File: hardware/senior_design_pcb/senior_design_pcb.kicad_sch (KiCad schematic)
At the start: 103 parts, among them J1 SBH11-PBPC-D05-ST-BK, J10 Conn_01x04_Socket, J11 2x08Rectangle-LED Matrix Conn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, J12 1x05JST - Joystick2 connector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, J13 UJ20-C-H-C-4-SMT-TR, J2 Conn_01x08_Pin, J3 Conn_01x02_Socket, J4 Conn_01x02_Socket, J5 1x05JST-Admin LCD Console Con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, J6 1x05JST - Joystick1 connector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, J9 Conn_01x04_Socket, SW3 1x02JST-Admin Console button 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, U1 KMR241GLFS, U10 KMR241GLFS, U2 STM32F091RCTx, U3 LD1117S33TR_SOT223, U4 KMR241GLFS, U5 USBLC6-2SC6Y, U6 2SA1873-GRTE85L_F, U7 2SA1873-GRTE85L_F, U8 2SA1873-GRTE85L_F, U9 KMR241GLFS

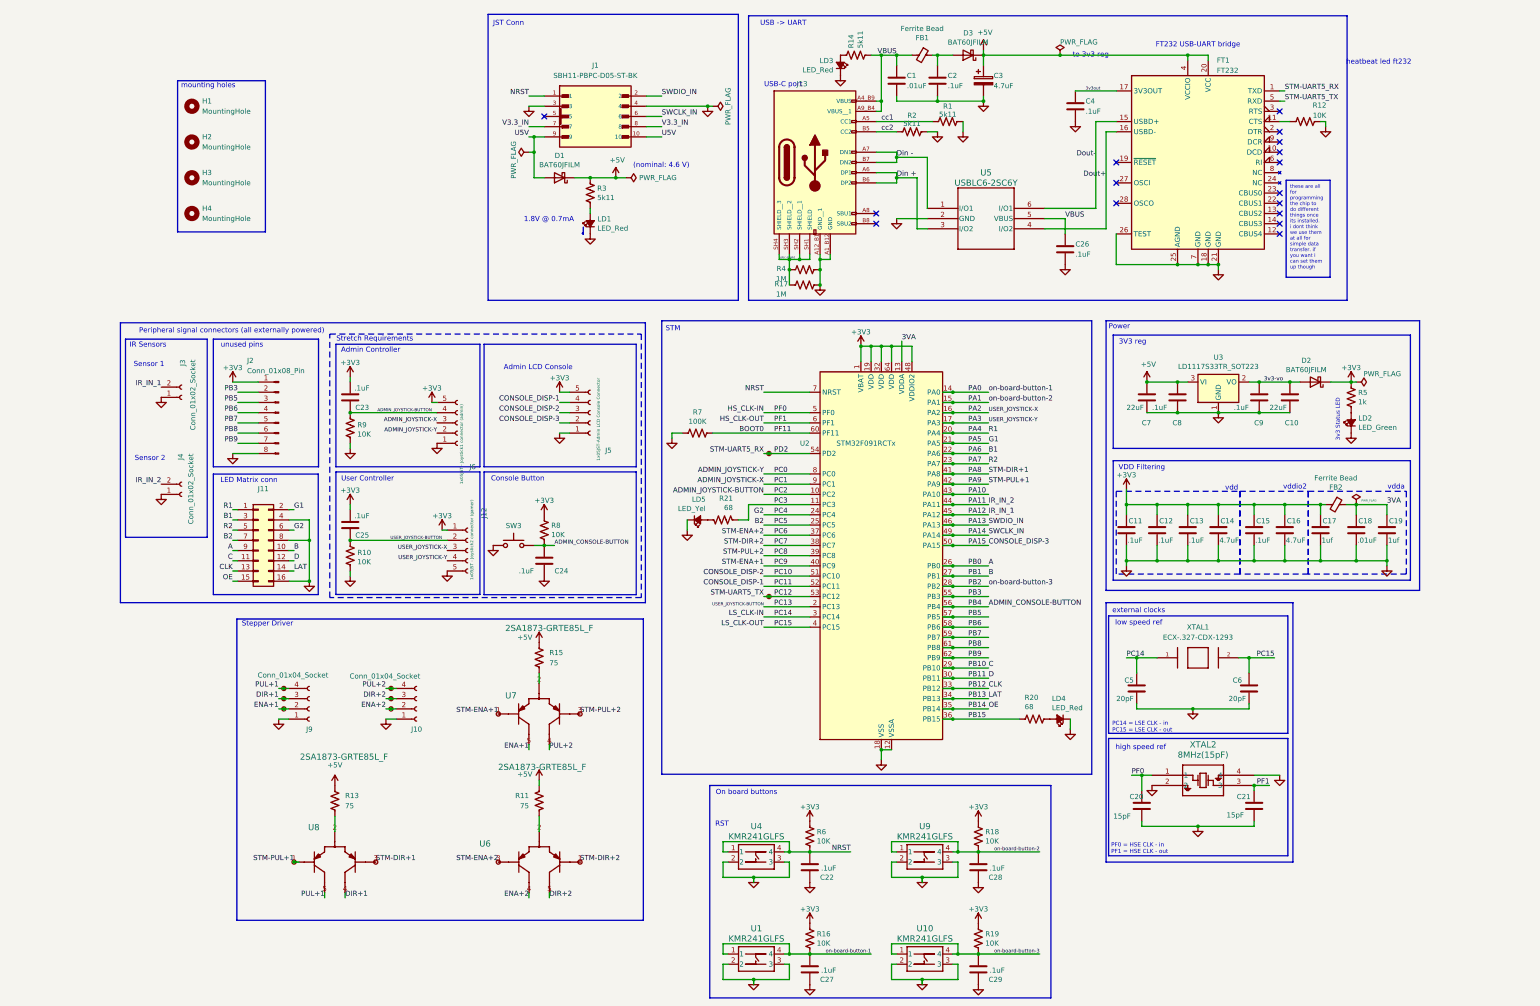
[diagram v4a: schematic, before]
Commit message: updated pcb
changes:
-all suggested from Setsuna & Shivam & presentation feedback
	-removed r4 and r17
	-kept multiple net names (following PCB Design Techniques - Spring 2025 from brightspace)
	-fixed XTAL1 missing connection
	-removed PWR_FLAG on GND
	-removed D2 - no need
	-increased via hole size (15 mil drill + 28 mil diameter)
	-kept chamfer (compared prices on jlc and pcbway and same price)
	-removed via on SW3
	-did not change traces beneath oscillators, everythings already routed but will keep in mind for the future
	-moved silkscreen names from off the board to on the board (we are still discussing decorative designs - if we include any)
	-kept FB since FB should be near source of noise and source of noise we are trying to prevent is from the USB-C. if we are misunderstanding this please let us know.
	-trace clearances updated, needed more with via size increase
	-moved silkscren + labeled pins
	-removed 3v connection from stlink. keeping only 5v

	-also, the led matrix connector somehow relapsed and changed to the 2x08 default header instead of a jtag type rectangular connector. updated and fixed :)

From prof. walters feedback:
-added back shield resistor
-added tvs diodes for joystick + buttons
-changed decoupling cap value
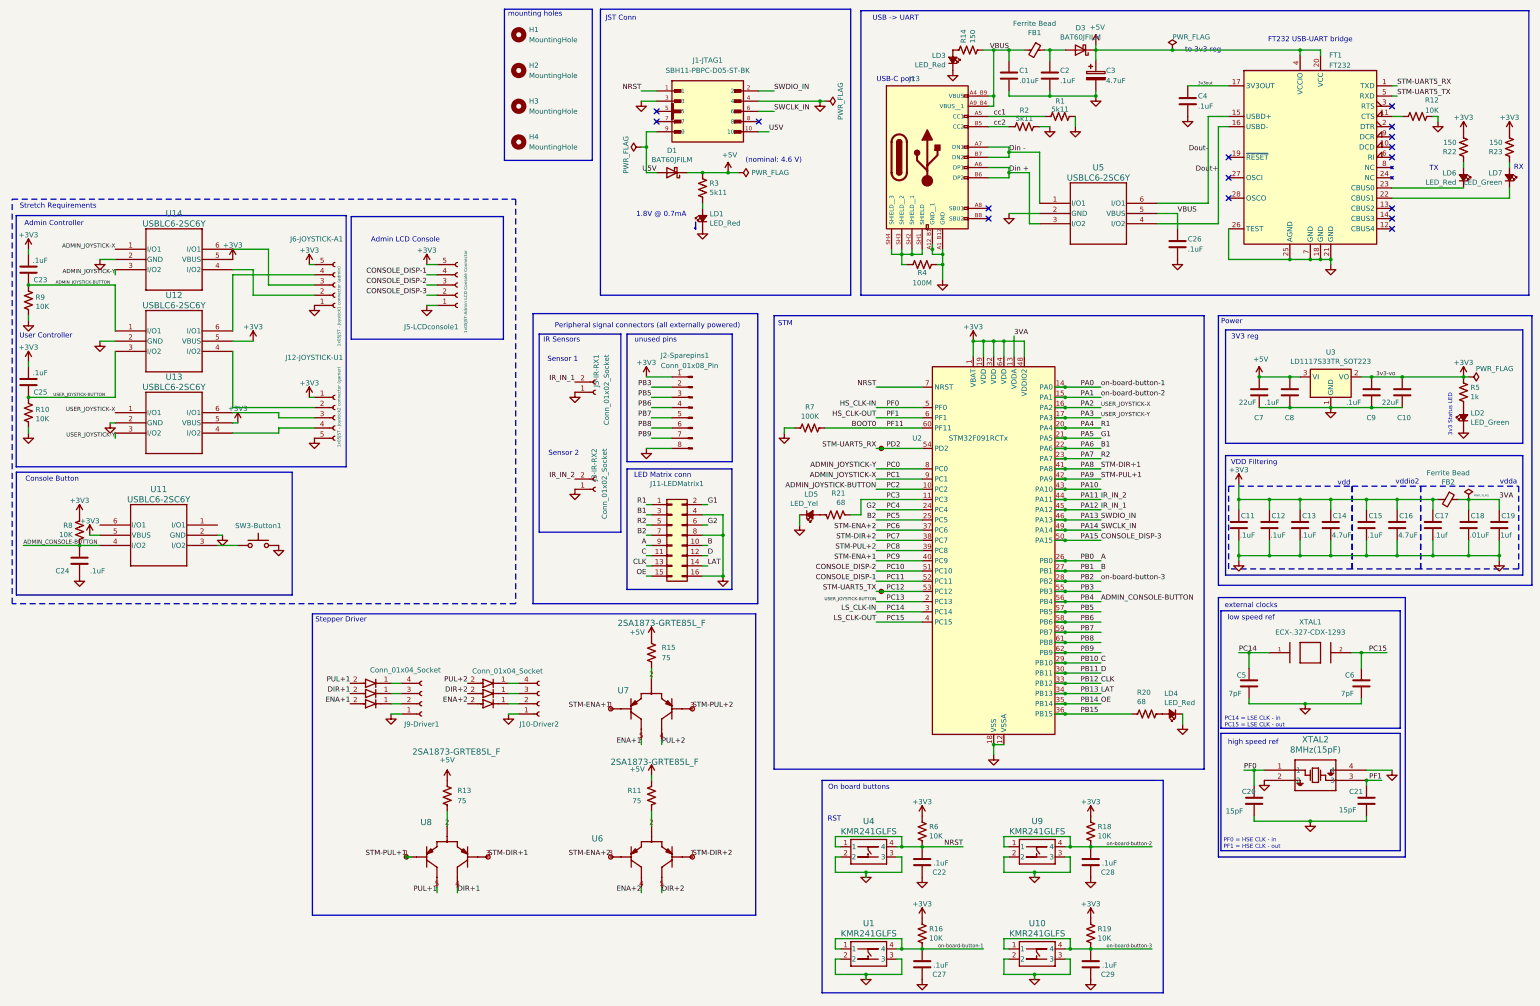
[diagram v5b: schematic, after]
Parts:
- removed D2: BAT60JFILM, Diode_SMD:D_SOD-323_HandSoldering, symbol Diode:BAT60A
- removed R17: 1M, Resistor_SMD:R_0805_2012Metric_Pad1.20x1.40mm_HandSolder, symbol Device:R_US
- removed TP1, TP2, TP3, TP4, TP5, TP6: TestPoint_Small, TestPoint:TestPoint_THTPad_D1.0mm_Drill0.5mm, symbol testpoint:TestPoint_Small
- added CR1, CR2, CR3, CR4, CR5, CR6: JAN1N4148UR-1, kicad_library:jan1n4148 smd diode-M, symbol jan1n4148 smd diode:JAN1N4148UR-1
- added LD6: LED_Red, LED_SMD:LED_0805_2012Metric, symbol Device:LED_Small_ALT
- added LD7: LED_Green, LED_SMD:LED_0805_2012Metric, symbol Device:LED_Small_ALT
- added R22, R23: 150, Resistor_SMD:R_0805_2012Metric_Pad1.20x1.40mm_HandSolder, symbol Device:R_US
- added U11, U12, U13, U14: USBLC6-2SC6Y, Sr_ Design:TVS-DIODE-USBLC6-2SC6Y, symbol TVS-DIODE-USBLC6-2SC6Y:USBLC6-2SC6Y
- C17: value 1uf -> .1uf
- C5, C6: value 20pF -> 7pF
- J11-LEDMatrix1: renamed from J11; footprint Connector_PinSocket_2.54mm:PinSocket_2x08_P2.54mm_Vertical -> General Library:jst-02x08 conn
- R14: value 5k11 -> 150
- R4: value 1M -> 100M
- TP10, TP11, TP12, TP7, TP8, TP9: footprint (none) -> TestPoint:TestPoint_THTPad_D1.0mm_Drill0.5mm
- XTAL1: footprint kicad_library:32KHZ-CLK-ECX1293 -> kicad_library:32khz clock - crystal
- renumbered J1 to J1-JTAG1, J10 to J10-Driver2, J12 to J12-JOYSTICK-U1, J2 to J2-Sparepins1, J3 to J3-IR-RX1, J4 to J3-IR-RX2, J5 to J5-LCDconsole1, J6 to J6-JOYSTICK-A1, J9 to J9-Driver1, SW3 to SW3-Button1
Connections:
- net 3v3-vo is gone; now on net +3V3: C10.1, C9.1, U3.2 (VO)
- net +3V3: now also R22.2, R23.2, U11.5 (VBUS), U12.5 (VBUS), U13.5 (VBUS), U14.5 (VBUS)
- net ADMIN_CONSOLE-BUTTON: now also U11.4 (I/O2); no longer SW3-Button1.2
- net ADMIN_JOYSTICK-BUTTON: now also U12.1 (I/O1); no longer J6-JOYSTICK-A1.4 (Pin_4)
- net ADMIN_JOYSTICK-X: now also U14.1 (I/O1); no longer J6-JOYSTICK-A1.3 (Pin_3)
- net ADMIN_JOYSTICK-Y: now also U14.3 (I/O2); no longer J6-JOYSTICK-A1.2 (Pin_2)
- net DIR+1: now also CR2.2; no longer J9-Driver1.3 (Pin_3)
- net DIR+2: now also CR5.2; no longer J10-Driver2.3 (Pin_3)
- net ENA+1: now also CR3.2; no longer J9-Driver1.2 (Pin_2)
- net ENA+2: now also CR6.2; no longer J10-Driver2.2 (Pin_2)
- net GND: now also R4.1, U11.2 (GND), U12.2 (GND), U13.2 (GND), U14.2 (GND); no longer R4.2
- net PA2: now also U13.1 (I/O1); no longer J12-JOYSTICK-U1.3 (Pin_3)
- net PA3: now also U13.3 (I/O2); no longer J12-JOYSTICK-U1.4 (Pin_4)
- net PC13: now also U12.3 (I/O2); no longer J12-JOYSTICK-U1.2 (Pin_2)
- net PUL+1: now also CR1.2; no longer J9-Driver1.4 (Pin_4)
- net PUL+2: now also CR4.2; no longer J10-Driver2.4 (Pin_4)
- net at FT1.22 (CBUS1): now also LD7.1 (K)
- net at FT1.23 (CBUS0): now also LD6.1 (K)
- net V3.3_IN: no longer names the net of J1-JTAG1.7
- net V3.3_IN: no longer J1-JTAG1.8
- net usbc-shield: no longer names the net of J13.SH1 (SHIELD), J13.SH2 (SHIELD__1), J13.SH3 (SHIELD__2), J13.SH4 (SHIELD__3)
- net usbc-shield: now also R4.2; no longer R4.1
- new net: J12-JOYSTICK-U1.2 (Pin_2), U12.4 (I/O2)
- new net: J6-JOYSTICK-A1.4 (Pin_4), U12.6 (I/O1)
- new net: J12-JOYSTICK-U1.4 (Pin_4), U13.4 (I/O2)
- new net: J12-JOYSTICK-U1.3 (Pin_3), U13.6 (I/O1)
- new net: SW3-Button1.2, U11.3 (I/O2)
- new net: CR6.1, J10-Driver2.2 (Pin_2)
- new net: J6-JOYSTICK-A1.2 (Pin_2), U14.4 (I/O2)
- new net: J6-JOYSTICK-A1.3 (Pin_3), U14.6 (I/O1)
- new net: CR5.1, J10-Driver2.3 (Pin_3)
- new net: CR2.1, J9-Driver1.3 (Pin_3)
- new net: CR4.1, J10-Driver2.4 (Pin_4)
- new net: CR1.1, J9-Driver1.4 (Pin_4)
- new net: LD6.2 (A), R22.1
- new net: LD7.2 (A), R23.1
- new net: CR3.1, J9-Driver1.2 (Pin_2)
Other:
- note added: "RX"
- note added: "TX"
- note removed: "heatbeat led ft232"
- moved on the sheet: C1, C10, C11, C12, C13, C14, C15, C16, C17, C18, C19, C2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
